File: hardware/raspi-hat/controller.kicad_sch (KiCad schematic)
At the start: 12 parts, among them J1 Conn_02x05_Counter_Clockwise, J5 USB3_A, U1 STSPIN32G4, Y1 Crystal_GND23_Small

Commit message: - updated pinout - updated cube mx
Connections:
- net shunt-amp1/OPOUT is gone; now on net shunt2_opout: U1.19 (PA6)
- net shunt-amp2/OPOUT is gone; now on net shunt3_opout: U1.24 (PB1)
- net ntc: now also U1.12 (PC3); no longer U1.17 (PA4)
- net v_bus_meas: now reaches C8.1, R21.2, R22.1, U1.13 (PA0)
- net shunt2_op-: now reaches U1.18 (PA5)
- net shunt2_opout: now reaches U1.21 (PC4)
- net shunt-amp/OP+ renamed shunt1_op+
- net shunt-amp/OP- renamed shunt1_op-
- net shunt-amp/OPOUT renamed shunt1_opout
- net shunt1_opout: now also U1.17 (PA4)
- net shunt-amp1/OP+ renamed shunt2_op+
- net shunt-amp1/OP- renamed shunt3_opout
- net shunt-amp2/OP+ renamed shunt3_op+
- net shunt-amp2/OP- renamed shunt3_op-
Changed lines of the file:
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@@
+	)
+	(junction
+		(at 181.61 86.36)
+		(diameter 0)
+		(color 0 0 0 0)
 	)
 	(junction
@@
 	)
 	(junction
+		(at 190.5 76.2)
+		(diameter 0)
+		(color 0 0 0 0)
+	)
+	(junction
 		(at 156.21 241.3)
 		(diameter 0)
@@
 	)
 	(junction
+		(at 184.15 119.38)
+		(diameter 0)
+		(color 0 0 0 0)
+	)
+	(junction
 		(at 149.86 241.3)
 		(diameter 0)
@@
 	(wire
 		(pts
-			(xy 104.14 76.2) (xy 207.01 76.2)
+			(xy 104.14 76.2) (xy 190.5 76.2)
 		)
 		(stroke
@@
 	(wire
 		(pts
-			(xy 127 86.36) (xy 207.01 86.36)
+			(xy 127 86.36) (xy 181.61 86.36)
 		)
 		(stroke
@@
 	(wire
 		(pts
+			(xy 207.01 162.56) (xy 184.15 162.56)
+		)
+		(stroke
+			(width 0)
+			(type default)
+		)
+	)
+	(wire
+		(pts
 			(xy 386.08 121.92) (xy 386.08 166.37)
 		)
@@
 	(wire
 		(pts
+			(xy 190.5 76.2) (xy 207.01 76.2)
+		)
+		(stroke
+			(width 0)
+			(type default)
+		)
+	)
+	(wire
+		(pts
+			(xy 204.47 157.48) (xy 207.01 157.48)
+		)
+		(stroke
+			(width 0)
+			(type default)
+		)
+	)
+	(wire
+		(pts
 			(xy 312.42 127) (xy 349.25 127)
 		)
@@
 	(wire
 		(pts
+			(xy 184.15 162.56) (xy 184.15 119.38)
+		)
+		(stroke
+			(width 0)
+			(type default)
+		)
+	)
+	(wire
+		(pts
 			(xy 254 170.18) (xy 254 26.67)
 		)
@@
 	(wire
 		(pts
-			(xy 135.89 119.38) (xy 207.01 119.38)
+			(xy 135.89 119.38) (xy 184.15 119.38)
 		)
 		(stroke
@@
 	(wire
 		(pts
-			(xy 116.84 104.14) (xy 132.08 104.14)
+			(xy 116.84 104.14) (xy 128.27 104.14)
 		)
 		(stroke
@@
 	(wire
 		(pts
+			(xy 181.61 86.36) (xy 207.01 86.36)
+		)
+		(stroke
+			(width 0)
+			(type default)
+		)
+	)
+	(wire
+		(pts
+			(xy 184.15 119.38) (xy 207.01 119.38)
+		)
+		(stroke
+			(width 0)
+			(type default)
+		)
+	)
+	(wire
+		(pts
 			(xy 307.34 163.83) (xy 307.34 123.19)
 		)
@@
 	(wire
 		(pts
+			(xy 207.01 160.02) (xy 181.61 160.02)
+		)
+		(stroke
+			(width 0)
+			(type default)
+		)
+	)
+	(wire
+		(pts
 			(xy 149.86 21.59) (xy 231.14 21.59)
 		)
@@
 	(wire
 		(pts
-			(xy 132.08 104.14) (xy 132.08 162.56)
+			(xy 128.27 104.14) (xy 128.27 83.82)
 		)
 		(stroke
@@
 	(wire
 		(pts
+			(xy 181.61 160.02) (xy 181.61 86.36)
+		)
+		(stroke
+			(width 0)
+			(type default)
+		)
+	)
+	(wire
+		(pts
 			(xy 127 105.41) (xy 127 86.36)
 		)
@@
 	(wire
 		(pts
-			(xy 132.08 162.56) (xy 207.01 162.56)
-		)
-		(stroke
-			(width 0)
-			(type default)
-		)
-	)
-	(wire
-		(pts
-			(xy 204.47 81.28) (xy 207.01 81.28)
+			(xy 128.27 83.82) (xy 207.01 83.82)
 		)
 		(stroke
@@
 	(wire
 		(pts
+			(xy 190.5 81.28) (xy 207.01 81.28)
+		)
+		(stroke
+			(width 0)
+			(type default)
+		)
+	)
+	(wire
+		(pts
 			(xy 95.25 26.67) (xy 107.95 26.67)
 		)
@@
 		(pts
 			(xy 125.73 88.9) (xy 207.01 88.9)
+		)
+		(stroke
+			(width 0)
+			(type default)
+		)
+	)
+	(wire
+		(pts
+			(xy 190.5 81.28) (xy 190.5 76.2)
 		)
 		(stroke
@@
 		)
 	)
+	(label "shunt1_op-"
+		(at 204.47 78.74 180)
+		(effects
+			(font
+				(size 1.27 1.27)
+			)
+			(justify right bottom)
+		)
+	)
 	(label "swd_io"
 		(at 204.47 104.14 180)
@@
 		)
 	)
+	(label "shunt2_op-"
+		(at 204.47 83.82 180)
+		(effects
+			(font
+				(size 1.27 1.27)
+			)
+			(justify right bottom)
+		)
+	)
 	(label "shunt3_h"
 		(at 389.89 142.24 0)
@@
 		)
 	)
+	(label "v_bus_meas"
+		(at 204.47 71.12 180)
+		(effects
+			(font
+				(size 1.27 1.27)
+			)
+			(justify right bottom)
+		)
+	)
+	(label "shunt2_opout"
+		(at 204.47 160.02 180)
+		(effects
+			(font
+				(size 1.27 1.27)
+			)
+			(justify right bottom)
+		)
+	)
 	(label "v_mc"
 		(at 171.45 46.99 180)
@@
 		)
 	)
+	(label "shunt3_opout"
+		(at 204.47 119.38 180)
+		(effects
+			(font
+				(size 1.27 1.27)
+			)
+			(justify right bottom)
+		)
+	)
+	(label "shunt1_opout"
+		(at 204.47 76.2 180)
+		(effects
+			(font
+				(size 1.27 1.27)
+			)
+			(justify right bottom)
+		)
+	)
+	(label "shunt2_op+"
+		(at 204.47 88.9 180)
+		(effects
+			(font
+				(size 1.27 1.27)
+			)
+			(justify right bottom)
+		)
+	)
 	(label "hall_3"
 		(at 191.77 170.18 0)
@@
 		)
 	)
+	(label "shunt3_opout"
+		(at 204.47 162.56 180)
+		(effects
+			(font
+				(size 1.27 1.27)
+			)
+			(justify right bottom)
+		)
+	)
 	(label "hall_2"
 		(at 191.77 167.64 0)
@@
 		)
 	)
+	(label "shunt3_op+"
+		(at 204.47 116.84 180)
+		(effects
+			(font
+				(size 1.27 1.27)
+			)
+			(justify right bottom)
+		)
+	)
 	(label "shunt2_l"
 		(at 77.47 105.41 180)
@@
 		)
 	)
+	(label "shunt2_opout"
+		(at 204.47 86.36 180)
+		(effects
+			(font
+				(size 1.27 1.27)
+			)
+			(justify right bottom)
+		)
+	)
 	(label "shunt1_l"
 		(at 389.89 135.89 0)
@@
 		)
 	)
+	(label "shunt3_op-"
+		(at 204.47 121.92 180)
+		(effects
+			(font
+				(size 1.27 1.27)
+			)
+			(justify right bottom)
+		)
+	)
 	(label "shunt2_h"
 		(at 389.89 138.43 0)
@@
 	)
 	(label "ntc"
-		(at 204.47 81.28 180)
+		(at 204.47 157.48 180)
 		(effects
 			(font
@@
 		)
 	)
+	(label "shunt1_op+"
+		(at 204.47 73.66 180)
+		(effects
+			(font
+				(size 1.27 1.27)
+			)
+			(justify right bottom)
+		)
+	)

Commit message: - added some more parts for temperature measurement - added capacitor
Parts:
- added D2, D4: SP0502BAHT, Package_TO_SOT_SMD:SOT-23, symbol Power_Protection:SP0502BAHT
- C8: value 100n -> 1u
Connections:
- net +5V: now also D2.1 (K)
- net GND: now also D2.3 (A), D4.3 (A)
- net hall_1: now also D4.1 (K)
- net hall_2: now also D4.2 (K)
- net hall_3: now also D2.2 (K)

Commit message: replaced usb connector for hall sensors with usbc
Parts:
- removed J5: USB3_A, Connector_USB:USB3_A_Receptacle_Wuerth_692122030100, symbol Connector:USB3_A
- added J7: USB_C_Receptacle, Connector_USB:USB_C_Receptacle_Molex_105450-0101, symbol Connector:USB_C_Receptacle
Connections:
- net +5V: now also J7.A4 (VBUS), J7.A9 (VBUS), J7.B4 (VBUS), J7.B9 (VBUS)
- net GND: now also J7.A1 (GND), J7.A12 (GND), J7.B1 (GND), J7.B12 (GND), J7.S1 (SHIELD)
- net hall_1: now also J7.A5 (CC1), J7.A8 (SBU1)
- net hall_2: now also J7.A7 (D-)
- net hall_3: now also J7.A6 (D+)

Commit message: fixed bom
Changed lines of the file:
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@@
-	)
-	(junction
-		(at 118.11 241.3)
-		(diameter 0)
-		(color 0 0 0 0)
 	)
 	(junction
@@
 	)
 	(junction
+		(at 120.65 160.02)
+		(diameter 0)
+		(color 0 0 0 0)
+	)
+	(junction
 		(at 53.34 171.45)
 		(diameter 0)
@@
 	)
 	(junction
-		(at 118.11 160.02)
-		(diameter 0)
-		(color 0 0 0 0)
-	)
-	(junction
 		(at 86.36 176.53)
 		(diameter 0)
@@
 		(color 0 0 0 0)
 	)
+	(junction
+		(at 120.65 241.3)
+		(diameter 0)
+		(color 0 0 0 0)
+	)
 	(wire
 		(pts
@@
 	(wire
 		(pts
+			(xy 120.65 241.3) (xy 149.86 241.3)
+		)
+		(stroke
+			(width 0)
+			(type default)
+		)
+	)
+	(wire
+		(pts
 			(xy 156.21 226.06) (xy 156.21 71.12)
 		)
@@
 	(wire
 		(pts
-			(xy 120.65 160.02) (xy 118.11 160.02)
-		)
-		(stroke
-			(width 0)
-			(type default)
-		)
-	)
-	(wire
-		(pts
 			(xy 383.54 119.38) (xy 387.35 119.38)
 		)
@@
 	(wire
 		(pts
-			(xy 118.11 160.02) (xy 95.25 160.02)
-		)
-		(stroke
-			(width 0)
-			(type default)
-		)
-	)
-	(wire
-		(pts
-			(xy 118.11 160.02) (xy 118.11 241.3)
+			(xy 95.25 160.02) (xy 120.65 160.02)
+		)
+		(stroke
+			(width 0)
+			(type default)
+		)
+	)
+	(wire
+		(pts
+			(xy 120.65 160.02) (xy 120.65 241.3)
 		)
 		(stroke
@@
 	(wire
 		(pts
-			(xy 118.11 241.3) (xy 149.86 241.3)
-		)
-		(stroke
-			(width 0)
-			(type default)
-		)
-	)
-	(wire
-		(pts
 			(xy 238.76 85.09) (xy 311.15 85.09)
 		)
@@
 	(wire
 		(pts
-			(xy 83.82 241.3) (xy 118.11 241.3)
-		)
-		(stroke
+			(xy 83.82 241.3) (xy 120.65 241.3)
+		)
+		(stroke

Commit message: updated hardware
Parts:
- added C18, C19, C20, C21, C22, C23, C24, C25, C26, C27, C28, C29, C30, C31, C32: 1u, Capacitor_SMD:C_0603_1608Metric, symbol Device:C
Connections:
- net GND: now also C18.2, C19.2, C20.2, C21.2, C22.2, C23.2, C24.2, C25.2, C26.2, C27.2, C28.2, C29.2, C30.2, C31.2, C32.2
- net phase_u: now also C18.1, C19.1, C20.1, C21.1, C22.1
- net phase_v: now also C28.1, C29.1, C30.1, C31.1, C32.1
- net phase_w: now also C23.1, C24.1, C25.1, C26.1, C27.1

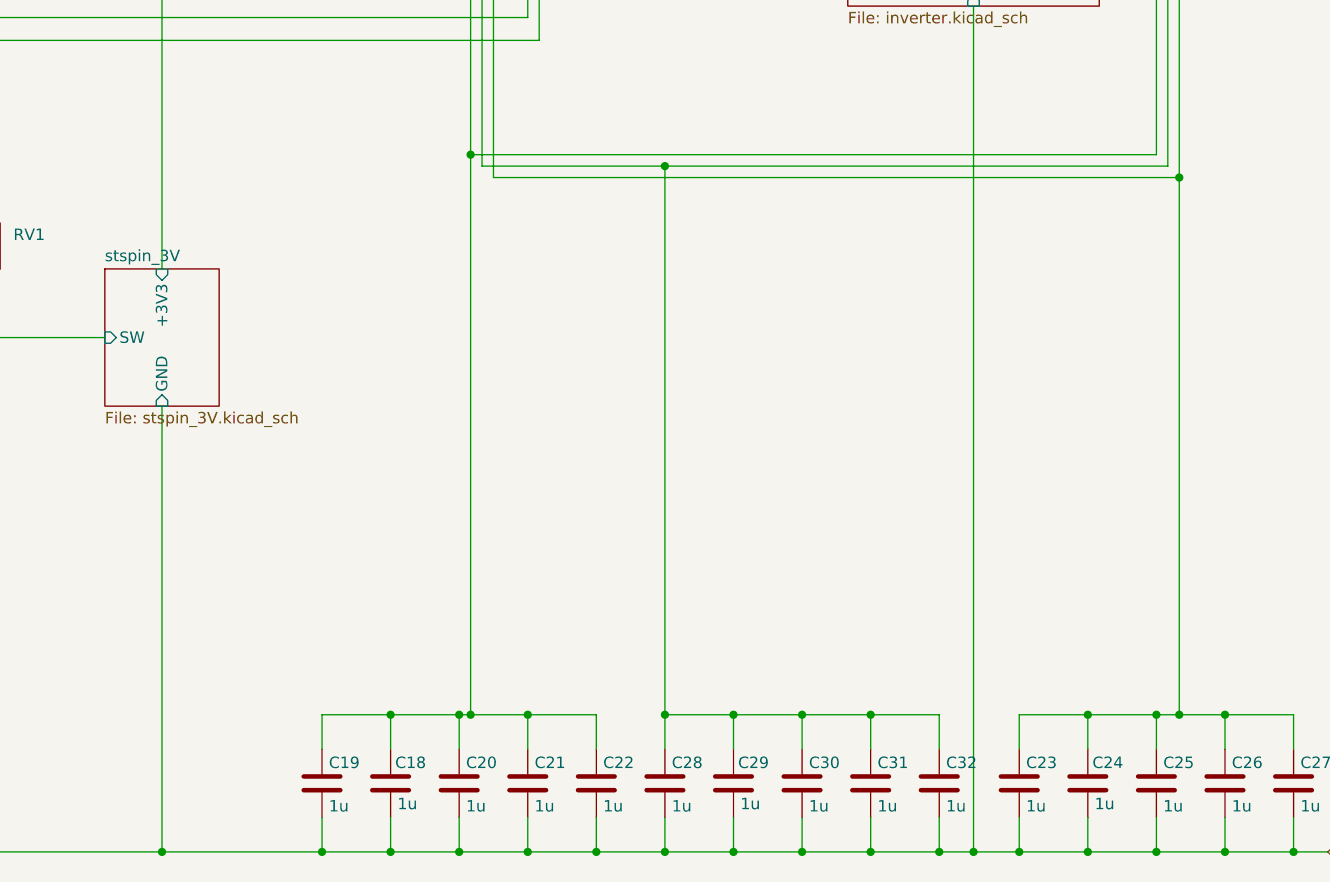
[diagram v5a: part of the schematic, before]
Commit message: removed capacitors that i couln't fit
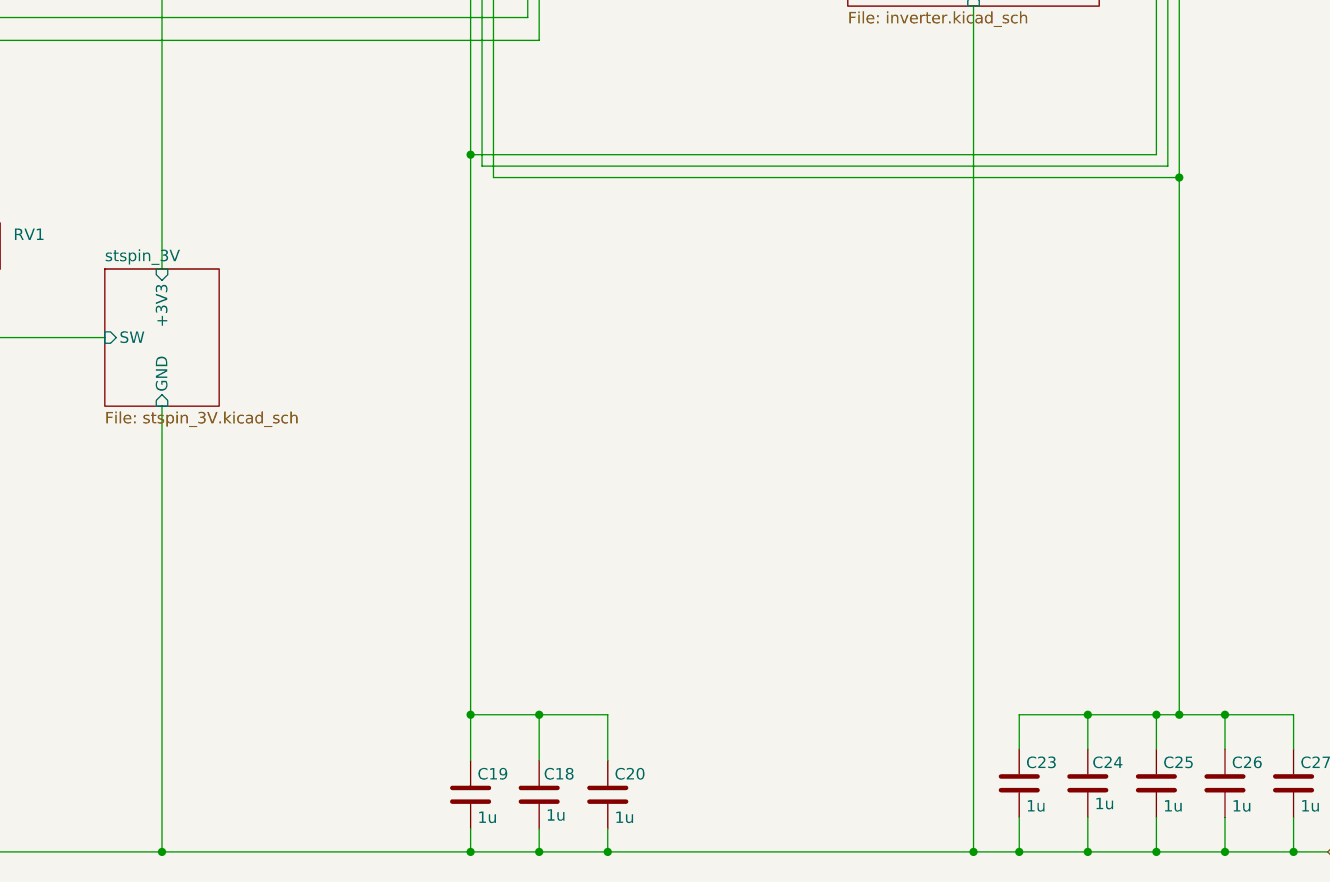
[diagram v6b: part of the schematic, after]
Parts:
- removed C21, C22, C28, C29, C30, C31, C32: 1u, Capacitor_SMD:C_0603_1608Metric, symbol Device:C
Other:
- moved on the sheet: C18, C19, C20
